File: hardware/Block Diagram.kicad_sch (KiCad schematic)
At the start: 0 parts

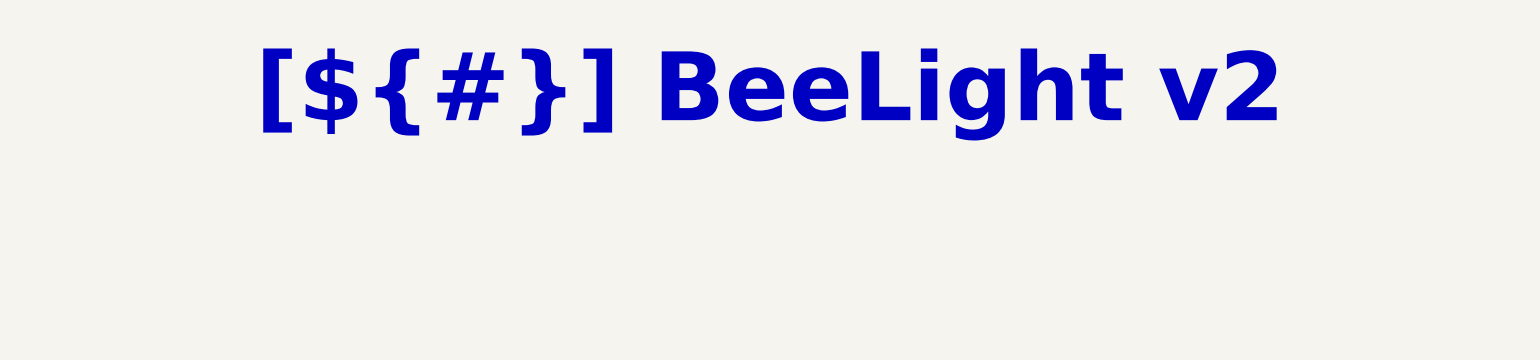
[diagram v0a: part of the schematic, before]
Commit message: Implement new CI/CD workflow
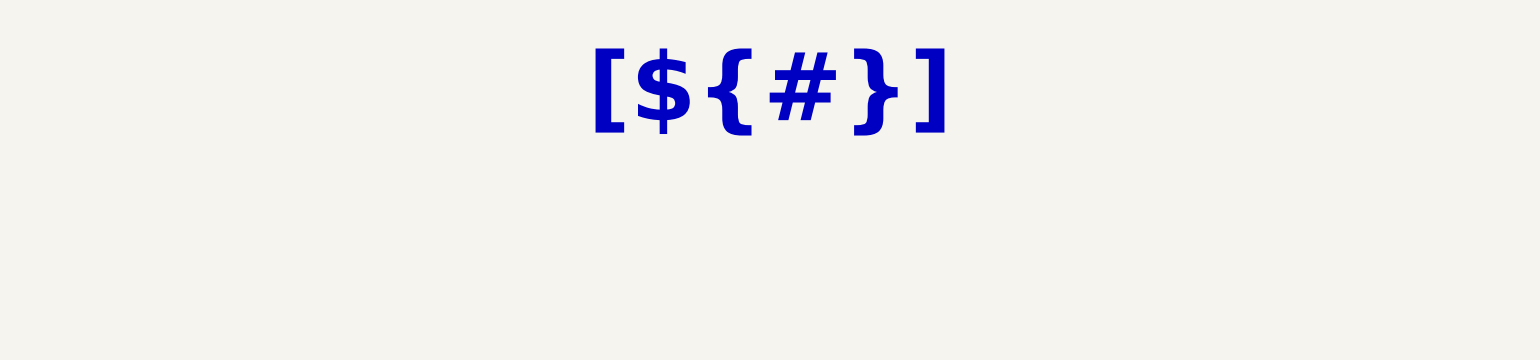
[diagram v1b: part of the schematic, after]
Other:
- title: BeeLight v2 -> (none)
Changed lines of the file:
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@@
 	(paper "A3")
 	(title_block
-		(title "BeeLight v2")
 		(date "2025-06-05")
 		(rev "${REVISION}")
@@
 			"AAAAAAAAAAAAAAAAAAAAAAAAAAAAAAAAAAAAAAAAAAAAAAAAAAAAAAAAAAAAAAAAAAAAAAAAAAAA"
 			"AAAAAAAAAAAAAAAAAAAAAAAAAAAAAAAAAAAAAAAAAAAAAAAAAAAAAAAAAAAAAAAAAAAAAAAAAAAA"
+			"AAAAAAAAAAAAAAAAAAAAAAAAAAAAAAAAAAAAAAAAAAAAAAAAAAAAAAAAAAAAAAAAAAAAAAAAAAAA"
+			"AAAAAAAAAAAAAAAAAAAAAAAAAAAAAAAAAAAAAAAAAAAAAAAAAAAAAAAAAAAAAAAAAAAAAAAAAAAA"
+			"AAAAAAAAAAAAAAAAAAAAAAAAAAAAAAAAAAAAAAAAAAAAAAAAAAAAAAAAAAAAAAAAAAAAAAAAAAAA"
+			"AAAAAAAAAAAAAAAAAAAAAAAAAAAAAAAAAAAAAAAAAAAAAAAAAAAAAAAAAAAAAAAAAAAAAAAAAAAA"
+			"AAAAAAAAAAAAAAAAAAAAAAAAAAAAAAAAAAAAAAAAAAAAAAAAAAAAAAAAAAAAAAAAAAAAAAAAAAAA"
+			"AAAAAAAAAAAAAAAAAAAAAAAAAAAAAAAAAAAAAAAAAAAAAAAAAAAAAAAAAAAAAAAAAAAAAAAAAAAA"
+			"AAAAAAAAAAAAAAAAAAAAAAAAAAAAAAAAAAAAAAAAAAAAAAAAAAAAAAAAAAAAAAAAAAAAAAAAAAAA"
+			"AAAAAAAAAAAAAAAAAAAAAAAAAAAAAAAAAAAAAAAAAAAAAAAAAAAAAAAAAAAAAAAAAAAAAAAAAAAA"
+			"AAAAAAAAAAAAAAAAAAAAAAAAAAAAAAAAAAAAAAAAAAAAAAAAAAAAAAAAAAAAAAAAAAAAAAAAAAAA"
+			"AAAAAAAAAAAAAAAAAAAAAAAAAAAAAAAAAAAAAAAAAAAAAAAAAAAAAAAAAAAAAAAAAAAAAAAAAAAA"
+			"AAAAAAAAAAAAAAAAAAAAAAAAAAAAAAAAAAAAAAAAAAAAAAAAAAAAAAAAAAAAAAAAAAAAAAAAAAAA"
+			"AAAAAAAAAAAAAAAAAAAAAAAAAAAAAAAAAAAAAAAAAAAAAAAAAAAAAAAAAAAAAAAAAAAAAAAAAAAA"
+			"AAAAAAAAAAAAAAAAAAAAAAAAAAAAAAAAAAAAAAAAAAAAAAAAAAAAAAAAAAAAAAAAAAAAAAAAAAAA"
+			"AAAAAAAAAAAAAAAAAAAAAAAAAAAAAAAAAAAAAAAAAAAAAAAAAAAAAAAAAAAAAAAAAAAAAAAAAAAA"
+			"AAAAAAAAAAAAAAAAAAAAAAAAAAAAAAAAAAAAAAAAAAAAAAAAAAAAAAAAAAAAAAAAAAAAAAAAAAAA"
+			"AAAAAAAAAAAAAAAAAAAAAAAAAAAAAAAAAAAAAAAAAAAAAAAAAAAAAAAAAAAAAAAAAAAAAAAAAAAA"
+			"AAAAAAAAAAAAAAAAAAAAAAAAAAAAAAAAAAAAAAAAAAAAAAAAAAAAAAAAAAAAAAAAAAAAAAAAAAAA"
+			"AAAAAAAAAAAAAAAAAAAAAAAAAAAAAAAAAAAAAAAAAAAAAAAAAAAAAAAAAAAAAAAAAAAAAAAAAAAA"
+			"AAAAAAAAAAAAAAAAAAAAAAAAAAAAAAAAAAAAAAAAAAAAAAAAAAAAAAAAAAAAAAAAAAAAAAAAAAAA"
+			"AAAAAAAAAAAAAAAAAAAAAAAAAAAAAAAAAAAAAAAAAAAAAAAAAAAAAAAAAAAAAAAAAAAAAAAAAAAA"
+			"AAAAAAAAAAAAAAAAAAAAAAAAAAAAAAAAAAAAAAAAAAAAAAAAAAAAAAAAAAAAAAAAAAAAAAAAAAAA"
+			"AAAAAAAAAAAAAAAAAAAAAAAAAAAAAAAAAAAAAAAAAAAAAAAAAAAAAAAAAAAAAAAAAAAAAAAAAAAA"
+			"AAAAAAAAAAAAAAAAAAAAAAAAAAAAAAAAAAAAAAAAAAAAAAAAAAAAAAAAAAAAAAAAAAAAAAAAAAAA"
+			"AAAAAAAAAAAAAAAAAAAAAAAAAAAAAAAAAAAAAAAAAAAAAAAAAAAAAAAAAAAAAAAAAAAAAAAAAAAA"
+			"AAAAAAAAAAAAAAAAAAAAAAAAAAAAAAAAAAAAAAAAAAAAAAAAAAAAAAAAAAAAAAAAAAAAAAAAAAAA"
+			"AAAAAAAAAAAAAAAAAAAAAAAAAAAAAAAAAAAAAAAAAAAAAAAAAAAAAAAAAAAAAAAAAAAAAAAAAAAA"
+			"AAAAAAAAAAAAAAAAAAAAAAAAAAAAAAAAAAAAAAAAAAAAAAAAAAAAAAAAAAAAAAAAAAAAAAAAAAAA"
+			"AAAAAAAAAAAAAAAAAAAAAAAAAAAAAAAAAAAAAAAAAAAAAAAAAAAAAAAAAAAAAAAAAAAAAAAAAAAA"
+			"AAAAAAAAAAAAAAAAAAAAAAAAAAAAAAAAAAAAAAAAAAAAAAAAAAAAAAAAAAAAAAAAAAAAAAAAAAAA"
+			"AAAAAAAAAAAAAAAAAAAAAAAAAAAAAAAAAAAAAAAAAAAAAAAAAAAAAAAAAAAAAAAAAAAAAAAAAAAA"
+			"AAAAAAAAAAAAAAAAAAAAAAAAAAAAAAAAAAAAAAAAAAAAAAAAAAAAAAAAAAAAAAAAAAAAAAAAAAAA"
+			"AAAAAAAAAAAAAAAAAAAAAAAAAAAAAAAAAAAAAAAAAAAAAAAAAAAAAAAAAAAAAAAAAAAAAAAAAAAA"
+			"AAAAAAAAAAAAAAAAAAAAAAAAAAAAAAAAAAAAAAAAAAAAAAAAAAAAAAAAAAAAAAAAAAAAAAAAAAAA"
+			"AAAAAAAAAAAAAAAAAAAAAAAAAAAAAAAAAAAAAAAAAAAAAAAAAAAAAAAAAAAAAAAAAAAAAAAAAG5l"
+			"ZChTTUFBX0dMU0xfNCkNCiNkZWZpbmUgbWFkKGEsIGIsIGMpIGZtYShhLCBiLCBjKQ0KI2RlZmlu"
+			"ZSBTTUFBR2F0aGVyKHRleCwgY29vcmQpIHRleHR1cmVHYXRoZXIodGV4LCBjb29yZCkNCiNlbHNl"
+			"DQojZGVmaW5lIG1hZChhLCBiLCBjKSAoYSAqIGIgKyBjKQ0KI2VuZGlmDQojZGVmaW5lIGZsb2F0"
+			"MiB2ZWMyDQojZGVmaW5lIGZsb2F0MyB2ZWMzDQojZGVmaW5lIGZsb2F0NCB2ZWM0DQojZGVmaW5l"
+			"IGludDIgaXZlYzINCiNkZWZpbmUgaW50MyBpdmVjMw0KI2RlZmluZSBpbnQ0IGl2ZWM0DQojZGVm"
+			"aW5lIGJvb2wyIGJ2ZWMyDQojZGVmaW5lIGJvb2wzIGJ2ZWMzDQojZGVmaW5lIGJvb2w0IGJ2ZWM0"
+			"DQojZW5kaWYNCg0KI2lmICFkZWZpbmVkKFNNQUFfSExTTF8zKSAmJiAhZGVmaW5lZChTTUFBX0hM"
+			"U0xfNCkgJiYgIWRlZmluZWQoU01BQV9ITFNMXzRfMSkgJiYgIWRlZmluZWQoU01BQV9HTFNMXzJf"
+			"MSkgJiYgIWRlZmluZWQoU01BQV9HTFNMXzMpICYmICFkZWZpbmVkKFNNQUFfR0xTTF80KSAmJiAh"
+			"ZGVmaW5lZChTTUFBX0NVU1RPTV9TTCkNCiNlcnJvciB5b3UgbXVzdCBkZWZpbmUgdGhlIHNoYWRp"
+			"bmcgbGFuZ3VhZ2U6IFNNQUFfSExTTF8qLCBTTUFBX0dMU0xfKiBvciBTTUFBX0NVU1RPTV9TTA0K"
+			"I2VuZGlmDQoNCi8vLS0tLS0tLS0tLS0tLS0tLS0tLS0tLS0tLS0tLS0tLS0tLS0tLS0tLS0tLS0t"
+			"LS0tLS0tLS0tLS0tLS0tLS0tLS0tLS0tLS0tLS0tLS0NCi8vIE1pc2MgZnVuY3Rpb25zDQoNCi8q"
+			"Kg0KICogR2F0aGVycyBjdXJyZW50IHBpeGVsLCBhbmQgdGhlIHRvcC1sZWZ0IG5laWdoYm9ycy4N"
+			"CiAqLw0KZmxvYXQzIFNNQUFHYXRoZXJOZWlnaGJvdXJzKGZsb2F0MiB0ZXhjb29yZCwNCiAgICAg"
+			"ICAgICAgICAgICAgICAgICAgICAgICBmbG9hdDQgb2Zmc2V0WzNdLA0KICAgICAgICAgICAgICAg"
+			"ICAgICAgICAgICAgIFNNQUFUZXh0dXJlMkQodGV4KSkgew0KICAgICNpZmRlZiBTTUFBR2F0aGVy"
+			"DQogICAgcmV0dXJuIFNNQUFHYXRoZXIodGV4LCB0ZXhjb29yZCArIFNNQUFfUlRfTUVUUklDUwAA"
+			"AAAAAAAAAAAAAAAAAAAAAAAAAAAAAAAAAAAAAAAAAAAAAAAAAAAAAAAAAAAAAAAAAAAAAAAAAAAA"
+			"AAAAAAAAAAAAAAAAAAAAAAAAAAAAAAAAAAAAAAAAAAAAAAAAAAAAAAAAAAAAAAAAAAAAAAAAAAAA"
